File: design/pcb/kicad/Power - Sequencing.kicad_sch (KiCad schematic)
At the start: 0 parts

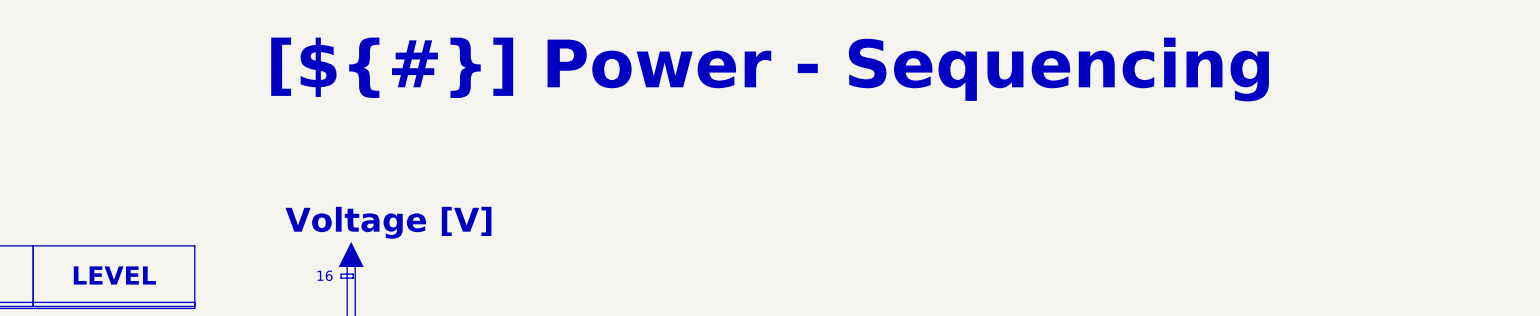
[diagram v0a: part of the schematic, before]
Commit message: Add LCD and STLink schematic sheets, update KiCad project files
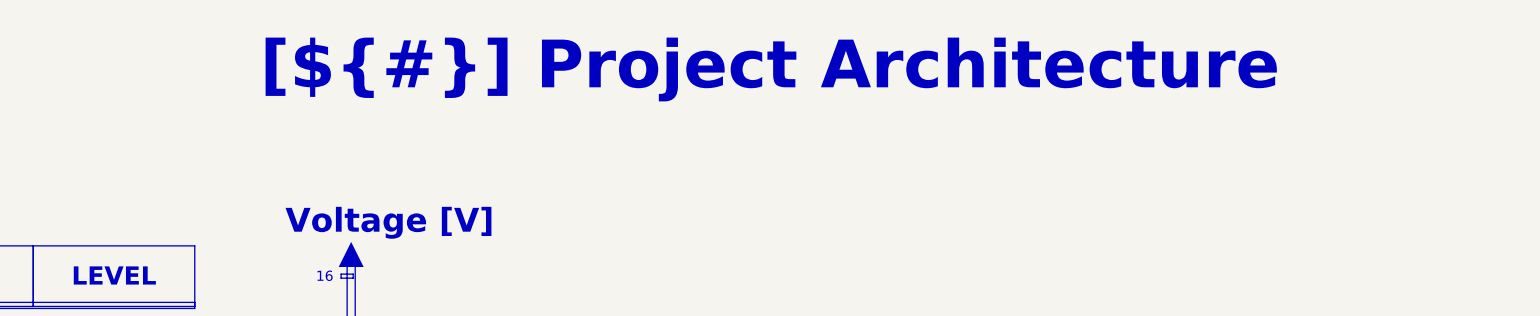
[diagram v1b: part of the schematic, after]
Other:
- title: Power - Sequencing -> Project Architecture
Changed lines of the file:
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@@
 	(paper "A4")
 	(title_block
-		(title "Power - Sequencing")
+		(title "Project Architecture")
 		(date "2025-01-12")
 		(rev "${REVISION}")
